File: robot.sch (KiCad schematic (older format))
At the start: 23 parts, among them P1 CONN_01X03, P2 CONN_01X03, P3 CONN_01X08, P4 CONN_01X08, P5 CONN_01X03, P7 CONN_01X08, Q1 BC548, U1 AMS1117-3V3, U2 ESP32-WROOM

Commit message: Ajuste na face do esp
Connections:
- net GND: now also Input-1.2 (P2); no longer Input-1.1 (P1)
- net VM: now also Output-1.1 (P1), U1.3 (VI); no longer Output+1.2 (P2)
- net Vin: now also Input-1.1 (P1); no longer Input+1.1 (P1), U1.3 (VI)
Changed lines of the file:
@@
 LIBS:valves
 LIBS:MCKPM-G1201A-K4037
-LIBS:AMS1117-3V3
-LIBS:arduino
-LIBS:misc
-LIBS:motor
-LIBS:mpu-6050
 LIBS:robot-cache
 EELAYER 25 0
@@
 	7350 3200 7350 3400
 Wire Wire Line
-	8050 2800 8050 5600
-Wire Wire Line
 	8050 2800 8800 2800
 $Comp
@@
 	0    1    1    0
 $EndComp
-Connection ~ 8050 5400
 $Comp
 L GND #PWR08
@@
 Wire Wire Line
 	1900 4800 3350 4800
-Wire Wire Line
-	3350 3350 3350 5300
 Wire Wire Line
 	3350 5300 3200 5300
@@
 	2450 2600 2450 2450
 Connection ~ 2450 2450
-Text GLabel 4150 5600 0    60   Input ~ 0
+Text GLabel 4150 5250 0    60   Input ~ 0
 Vin
 Text GLabel 3200 5350 2    60   Input ~ 0
@@
 L GND #PWR010
 U 1 1 5B5B63B8
-P 4150 5250
-F 0 "#PWR010" H 4150 5000 50  0001 C CNN
-F 1 "GND" H 4150 5100 50  0000 C CNN
-F 2 "" H 4150 5250 50  0000 C CNN
-F 3 "" H 4150 5250 50  0000 C CNN
-	1    4150 5250
-	0    1    1    0
-$EndComp
-Wire Wire Line
-	8050 5600 5300 5600
+P 4150 5350
+F 0 "#PWR010" H 4150 5100 50  0001 C CNN
+F 1 "GND" H 4150 5200 50  0000 C CNN
+F 2 "" H 4150 5350 50  0000 C CNN
+F 3 "" H 4150 5350 50  0000 C CNN
+	1    4150 5350
+	0    1    1    0
+$EndComp
 $Comp
 L GND #PWR011
@@
 	1    0    0    -1
 $EndComp
-Wire Wire Line
-	3350 3350 3650 3350
 Connection ~ 3350 4800
 $Comp
@@
 	-1   0    0    1
 $EndComp
+Wire Wire Line
+	3350 4800 3350 5300
+Wire Wire Line
+	6100 4950 3550 4950
+Wire Wire Line
+	3550 4950 3550 3350
+Connection ~ 3550 3350
+Wire Wire Line
+	3550 3350 3650 3350
+Wire Wire Line
+	5300 5300 8050 5300
+Connection ~ 8050 5300
+Wire Wire Line
+	6100 4950 6100 5300
+Connection ~ 6100 5300
+Wire Wire Line
+	8050 5300 8050 2800
 $EndSCHEMATC

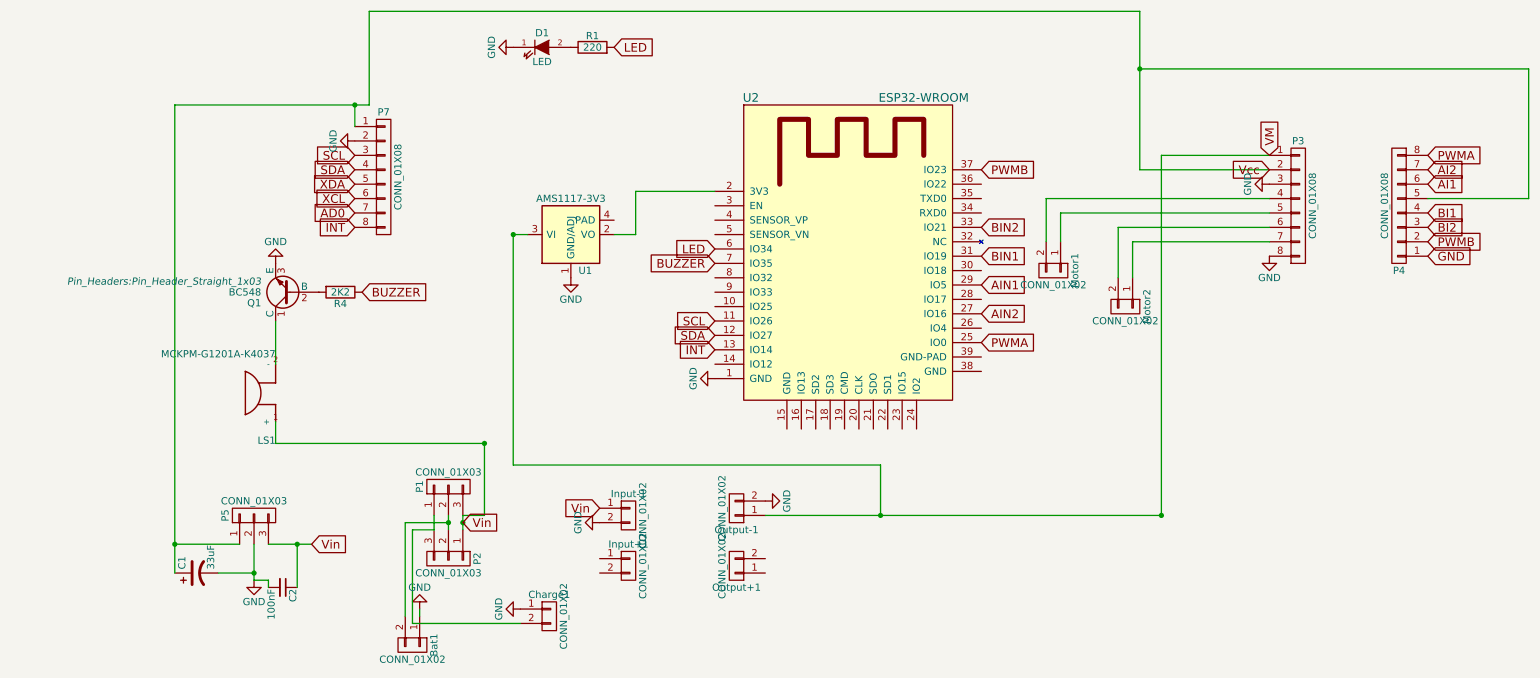
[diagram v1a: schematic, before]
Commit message: mudanças na dimensão da placa.
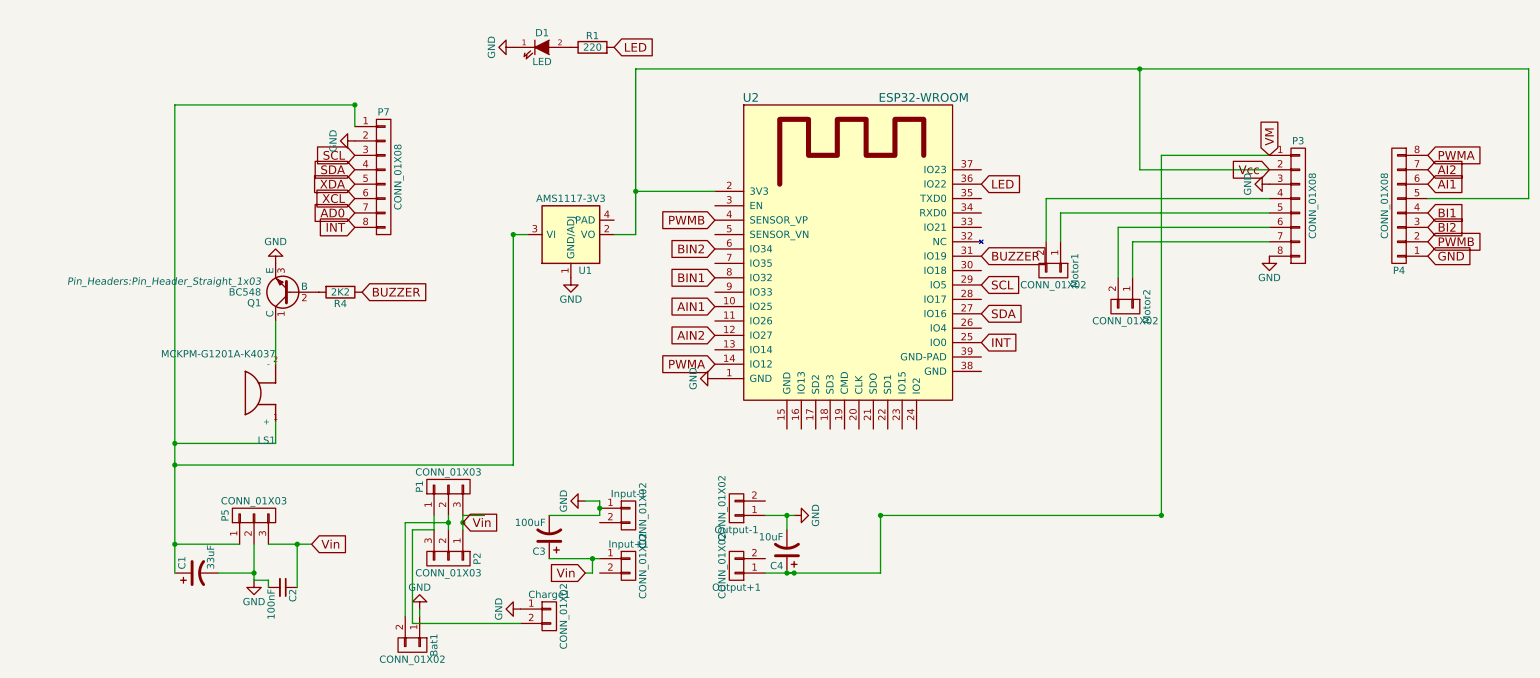
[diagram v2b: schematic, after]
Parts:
- added C3: 100uF, Capacitors_ThroughHole:C_Radial_D5_L11_P2.5, symbol CP1
- added C4: 10uF, Capacitors_ThroughHole:C_Radial_D5_L11_P2.5, symbol CP1
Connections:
- net AIN1: now also U2.10 (IO25); no longer U2.29 (IO5)
- net AIN2: now also U2.12 (IO27); no longer U2.27 (IO16)
- net BIN1: now also U2.8 (IO32); no longer U2.31 (IO19)
- net BIN2: now also U2.6 (IO34); no longer U2.33 (IO21)
- net BUZZER: now also U2.31 (IO19); no longer U2.7 (IO35)
- net GND: now also Input-1.1 (P1), Output-1.1 (P1), C3.2, C4.2; no longer Input-1.2 (P2), Output-1.2 (P2)
- net INT: now also U2.25 (IO0); no longer U2.13 (IO14)
- net LED: now also U2.36 (IO22); no longer U2.6 (IO34)
- net PWMA: now also U2.14 (IO12); no longer U2.25 (IO0)
- net PWMB: now also U2.4 (SENSOR_VP); no longer U2.37 (IO23)
- net SCL: now also U2.29 (IO5); no longer U2.11 (IO26)
- net SDA: now also U2.27 (IO16); no longer U2.12 (IO27)
- net VM: now also Output+1.1 (P1), C4.1; no longer Output-1.1 (P1), U1.3 (VI)
- net Vcc: now also U1.2 (VO), U2.2 (3V3); no longer C1.1, P5.1 (P1), P7.1 (P1)
- net Vin: now also Input+1.1 (P1), C3.1; no longer Input-1.1 (P1), LS1.1 (+)
- new net: C1.1, LS1.1 (+), P5.1 (P1), P7.1 (P1), U1.3 (VI)
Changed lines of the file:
@@
 LIBS:contrib
 LIBS:valves
-LIBS:MCKPM-G1201A-K4037
 LIBS:robot-cache
 EELAYER 25 0
@@
 	0    1    1    0
 $EndComp
-Wire Wire Line
-	1200 2450 2550 2450
 $Comp
 L CONN_01X02 Bat1
@@
 	0    1    1    0
 $EndComp
-Text GLabel 6800 2900 2    60   Input ~ 0
+Text GLabel 4950 3250 0    60   Input ~ 0
 PWMB
-Text GLabel 6800 3500 2    60   Input ~ 0
+Text GLabel 4950 3650 0    60   Input ~ 0
 BIN1
-Text GLabel 6800 3300 2    60   Input ~ 0
+Text GLabel 4950 3450 0    60   Input ~ 0
 BIN2
-Text GLabel 6800 3700 2    60   Input ~ 0
+Text GLabel 4950 3850 0    60   Input ~ 0
 AIN1
-Text GLabel 6800 3900 2    60   Input ~ 0
+Text GLabel 4950 4050 0    60   Input ~ 0
 AIN2
-Text GLabel 6800 4100 2    60   Input ~ 0
+Text GLabel 4950 4250 0    60   Input ~ 0
 PWMA
-Wire Wire Line
-	2550 2450 2550 1800
-Wire Wire Line
-	2550 1800 7900 1800
-Wire Wire Line
-	7900 1800 7900 2900
 Wire Wire Line
 	7900 2900 8800 2900
@@
 Text GLabel 4250 2050 2    60   Input ~ 0
 LED
-Text GLabel 4950 3450 0    60   Input ~ 0
+Text GLabel 6800 3000 2    60   Input ~ 0
 LED
-Text GLabel 4950 3550 0    60   Input ~ 0
+Text GLabel 6800 3500 2    60   Input ~ 0
 BUZZER
-Text GLabel 4950 4050 0    60   Input ~ 0
+Text GLabel 6800 3900 2    60   Input ~ 0
 SDA
-Text GLabel 4950 3950 0    60   Input ~ 0
+Text GLabel 6800 3700 2    60   Input ~ 0
 SCL
-Text GLabel 4950 4150 0    60   Input ~ 0
+Text GLabel 6800 4100 2    60   Input ~ 0
 INT
 Wire Wire Line
-	7900 2200 10600 2200
+	4400 2200 10600 2200
 Wire Wire Line
 	10600 2200 10600 3100
@@
 $EndComp
 Wire Wire Line
-	1900 4800 3350 4800
-Wire Wire Line
 	3350 5300 3200 5300
 $Comp
@@
 	2450 2600 2450 2450
 Connection ~ 2450 2450
-Text GLabel 4150 5250 0    60   Input ~ 0
+Text GLabel 4050 5700 0    60   Input ~ 0
 Vin
 Text GLabel 3200 5350 2    60   Input ~ 0
@@
 L GND #PWR010
 U 1 1 5B5B63B8
-P 4150 5350
-F 0 "#PWR010" H 4150 5100 50  0001 C CNN
-F 1 "GND" H 4150 5200 50  0000 C CNN
-F 2 "" H 4150 5350 50  0000 C CNN
-F 3 "" H 4150 5350 50  0000 C CNN
-	1    4150 5350
+P 4050 5200
+F 0 "#PWR010" H 4050 4950 50  0001 C CNN
+F 1 "GND" H 4050 5050 50  0000 C CNN
+F 2 "" H 4050 5200 50  0000 C CNN
+F 3 "" H 4050 5200 50  0000 C CNN
+	1    4050 5200
 	0    1    1    0
 $EndComp
@@
 L GND #PWR011
 U 1 1 5B5B64E5
-P 5300 5200
-F 0 "#PWR011" H 5300 4950 50  0001 C CNN
-F 1 "GND" H 5300 5050 50  0000 C CNN
-F 2 "" H 5300 5200 50  0000 C CNN
-F 3 "" H 5300 5200 50  0000 C CNN
-	1    5300 5200
+P 5500 5300
+F 0 "#PWR011" H 5500 5050 50  0001 C CNN
+F 1 "GND" H 5500 5150 50  0000 C CNN
+F 2 "" H 5500 5300 50  0000 C CNN
+F 3 "" H 5500 5300 50  0000 C CNN
+	1    5500 5300
 	0    -1   -1   0
 $EndComp
@@
 	1    0    0    -1
 $EndComp
-Connection ~ 3350 4800
 $Comp
 L GND #PWR012
@@
 $EndComp
 Wire Wire Line
-	4250 3350 4400 3350
-Wire Wire Line
-	4400 3350 4400 3050
+	4400 3350 4250 3350
+Wire Wire Line
+	4400 2200 4400 3350
 Wire Wire Line
 	4400 3050 4950 3050
@@
 $EndComp
 Wire Wire Line
-	3350 4800 3350 5300
-Wire Wire Line
-	6100 4950 3550 4950
-Wire Wire Line
 	3550 4950 3550 3350
 Connection ~ 3550 3350
 Wire Wire Line
 	3550 3350 3650 3350
-Wire Wire Line
-	5300 5300 8050 5300
 Connection ~ 8050 5300
-Wire Wire Line
-	6100 4950 6100 5300
 Connection ~ 6100 5300
 Wire Wire Line
 	8050 5300 8050 2800
+Wire Wire Line
+	6100 5700 5300 5700
+Wire Wire Line
+	6100 5300 8050 5300
+$Comp
+L CP1 C4
+U 1 1 5B69B226
+P 5450 5550
+F 0 "C4" H 5475 5650 50  0000 L CNN
+F 1 "10uF" H 5475 5450 50  0000 L CNN
+F 2 "Capacitors_ThroughHole:C_Radial_D5_L11_P2.5" H 5450 5550 50  0001 C CNN
+F 3 "" H 5450 5550 50  0000 C CNN
+	1    5450 5550
+	-1   0    0    1
+$EndComp
+Wire Wire Line
+	5300 5300 5500 5300
+Wire Wire Line
+	5450 5400 5450 5300
+Connection ~ 5450 5300
+$Comp
+L CP1 C3
+U 1 1 5B69B70A
+P 3800 5450
+F 0 "C3" H 3825 5550 50  0000 L CNN
+F 1 "100uF" H 3825 5350 50  0000 L CNN
+F 2 "Capacitors_ThroughHole:C_Radial_D5_L11_P2.5" H 3800 5450 50  0001 C CNN
+F 3 "" H 3800 5450 50  0000 C CNN
+	1    3800 5450
+	-1   0    0    1
+$EndComp
+Wire Wire Line
+	4150 5300 3800 5300
+Wire Wire Line
+	4150 5200 4150 5300
+Wire Wire Line
+	4050 5200 4150 5200
+Connection ~ 4150 5250
+Wire Wire Line
+	4150 5600 3800 5600
+Wire Wire Line
+	4050 5700 4100 5700
+Wire Wire Line
+	4100 5700 4100 5600
+Connection ~ 4100 5600
+Wire Wire Line
+	5500 5700 5450 5700
+Connection ~ 5450 5700
+Connection ~ 5500 5700
+Connection ~ 4400 3050
+Wire Wire Line
+	7900 2900 7900 2200
+Wire Wire Line
+	2450 2450 1200 2450
+Wire Wire Line
+	6100 5300 6100 5700
+Wire Wire Line
+	3550 4950 1200 4950
+Connection ~ 1200 4950
+Wire Wire Line
+	1900 4800 1200 4800
+Connection ~ 1200 4800
 $EndSCHEMATC

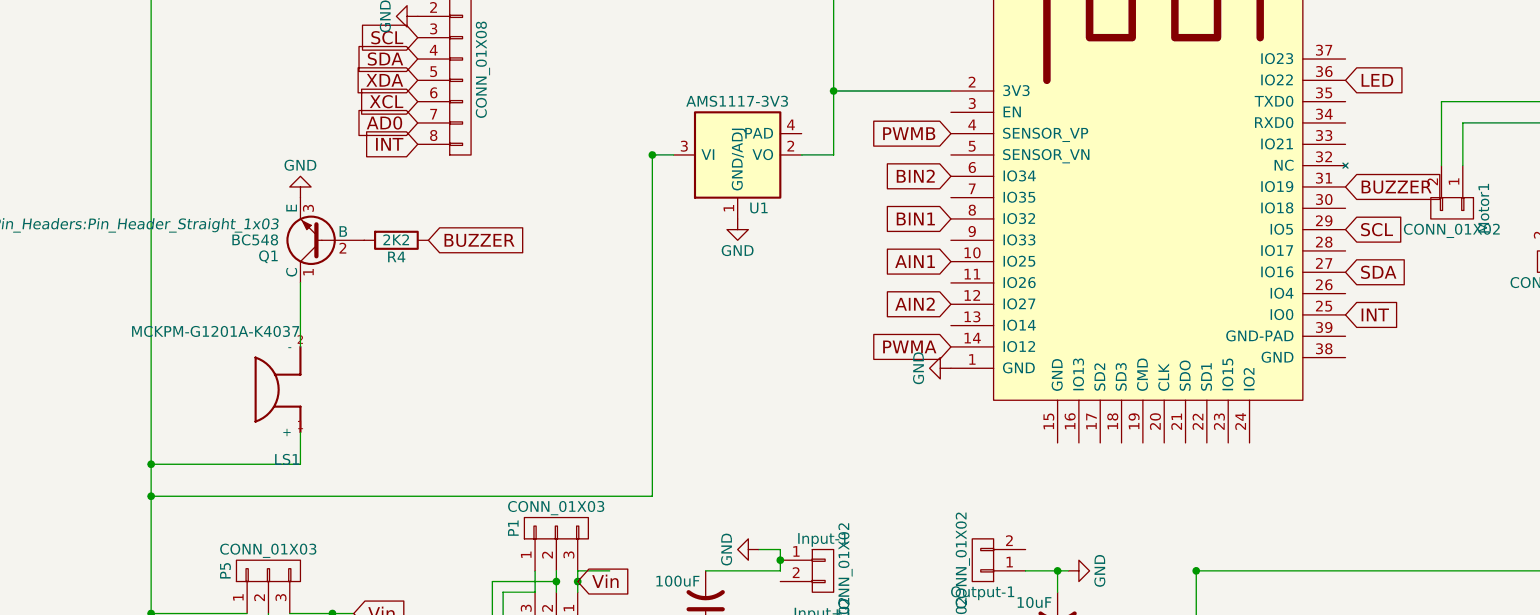
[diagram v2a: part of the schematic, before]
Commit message: corrigir gnd da ponte H
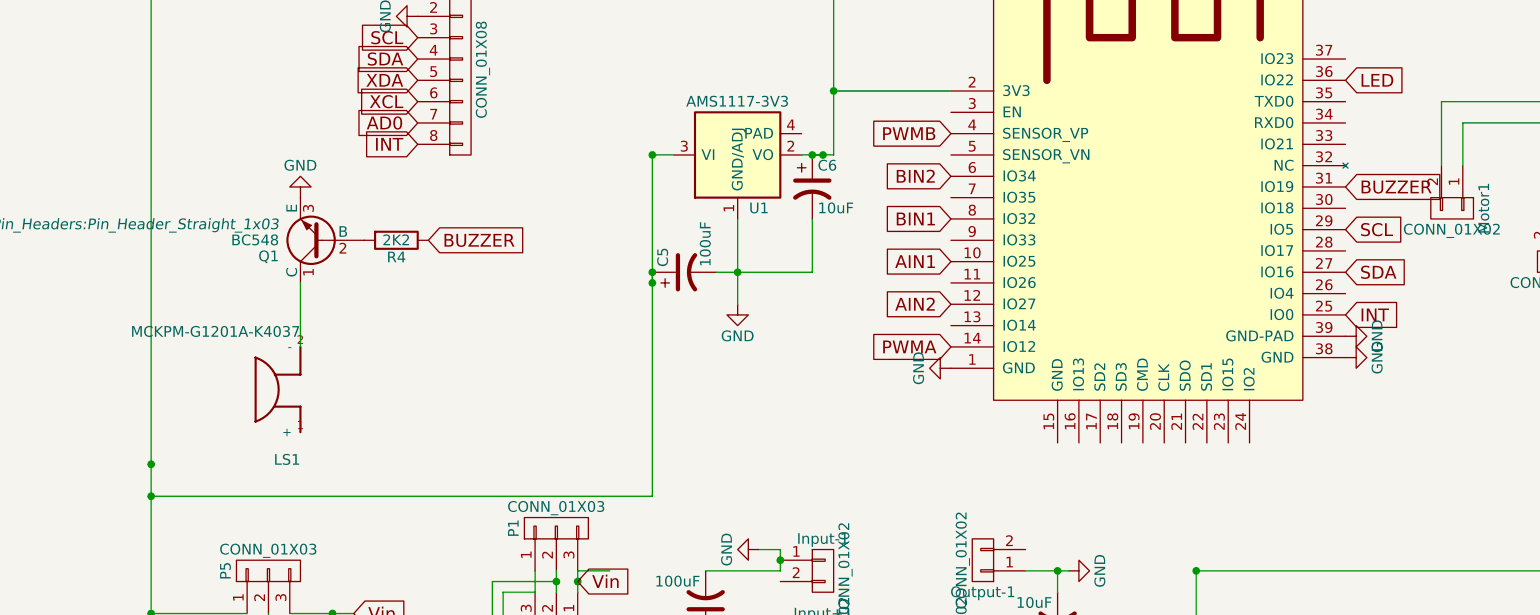
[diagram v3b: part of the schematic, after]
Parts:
- added C5: 100uF, Capacitors_ThroughHole:C_Radial_D5_L11_P2.5, symbol CP1
- added C6: 10uF, Capacitors_ThroughHole:C_Radial_D5_L11_P2.5, symbol CP1
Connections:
- net GND: now also U2.38 (GND), U2.39 (GND-PAD), C5.2, C6.2
- net Vcc: now also C6.1
- net at C1.1, P5.1 (P1), P7.1 (P1)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: now also C5.1; no longer LS1.1 (+)
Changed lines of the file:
@@
 Text GLabel 2500 3750 2    60   Input ~ 0
 BUZZER
-Wire Wire Line
-	1900 4800 1900 4650
 Text GLabel 4250 2050 2    60   Input ~ 0
 LED
@@
 L GND #PWR012
 U 1 1 5B5B7169
-P 3950 3650
-F 0 "#PWR012" H 3950 3400 50  0001 C CNN
-F 1 "GND" H 3950 3500 50  0000 C CNN
-F 2 "" H 3950 3650 50  0000 C CNN
-F 3 "" H 3950 3650 50  0000 C CNN
-	1    3950 3650
+P 3950 4050
+F 0 "#PWR012" H 3950 3800 50  0001 C CNN
+F 1 "GND" H 3950 3900 50  0000 C CNN
+F 2 "" H 3950 4050 50  0000 C CNN
+F 3 "" H 3950 4050 50  0000 C CNN
+	1    3950 4050
 	1    0    0    -1
 $EndComp
@@
 	3550 4950 1200 4950
 Connection ~ 1200 4950
-Wire Wire Line
-	1900 4800 1200 4800
 Connection ~ 1200 4800
+$Comp
+L GND #PWR013
+U 1 1 5B6B63B3
+P 6800 4300
+F 0 "#PWR013" H 6800 4050 50  0001 C CNN
+F 1 "GND" H 6800 4150 50  0000 C CNN
+F 2 "" H 6800 4300 50  0000 C CNN
+F 3 "" H 6800 4300 50  0000 C CNN
+	1    6800 4300
+	0    -1   -1   0
+$EndComp
+$Comp
+L GND #PWR014
+U 1 1 5B6B64B2
+P 6800 4200
+F 0 "#PWR014" H 6800 3950 50  0001 C CNN
+F 1 "GND" H 6800 4050 50  0000 C CNN
+F 2 "" H 6800 4200 50  0000 C CNN
+F 3 "" H 6800 4200 50  0000 C CNN
+	1    6800 4200
+	0    -1   -1   0
+$EndComp
+$Comp
+L CP1 C5
+U 1 1 5B6B67F4
+P 3700 3900
+F 0 "C5" H 3725 4000 50  0000 L CNN
+F 1 "100uF" H 3725 3800 50  0000 L CNN
+F 2 "Capacitors_ThroughHole:C_Radial_D5_L11_P2.5" H 3700 3900 50  0001 C CNN
+F 3 "" H 3700 3900 50  0000 C CNN
+	1    3700 3900
+	0    -1   -1   0
+$EndComp
+$Comp
+L CP1 C6
+U 1 1 5B6B689E
+P 4300 3500
+F 0 "C6" H 4325 3600 50  0000 L CNN
+F 1 "10uF" H 4325 3400 50  0000 L CNN
+F 2 "Capacitors_ThroughHole:C_Radial_D5_L11_P2.5" H 4300 3500 50  0001 C CNN
+F 3 "" H 4300 3500 50  0000 C CNN
+	1    4300 3500
+	1    0    0    -1
+$EndComp
+Wire Wire Line
+	3950 4050 3950 3650
+Wire Wire Line
+	3850 3900 4300 3900
+Connection ~ 3950 3900
+Wire Wire Line
+	4300 3900 4300 3650
+Wire Wire Line
+	3550 3950 3550 3900
+Connection ~ 3550 3900
+Connection ~ 3550 3950
+Wire Wire Line
+	4350 3350 4300 3350
+Connection ~ 4300 3350
+Connection ~ 4350 3350
 $EndSCHEMATC
